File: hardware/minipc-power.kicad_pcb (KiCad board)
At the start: 4 copper layers, 52 x 36 mm, 106 parts, among them J1 USB-C HRO TYPE-C-31-M-12, J10 VSYS (switch), J11 CHG, J12 PG_CHG, J13 VBAT_SENSE, J14 3V3_PG, J15 GND, J16 GND, J17 GND, J2 BAT+, J3 BAT-, J4 NTC, J5 NTC-, J6 +12V OUT, J7 +5V OUT, J8 +3V3 OUT, J9 EN (switch), Q1 DMN1004UFV, Q2 DMN1004UFV, Q3 DMN1004UFV, Q4 CSD25404Q3, Q5 CSD25404Q3, Q6 2N7002, U1 CH224Q, U2 BQ25606, U3 HY2113-MB1A, U4 TPS61178, U5 TPS61088-Q1, U6 TPS63802

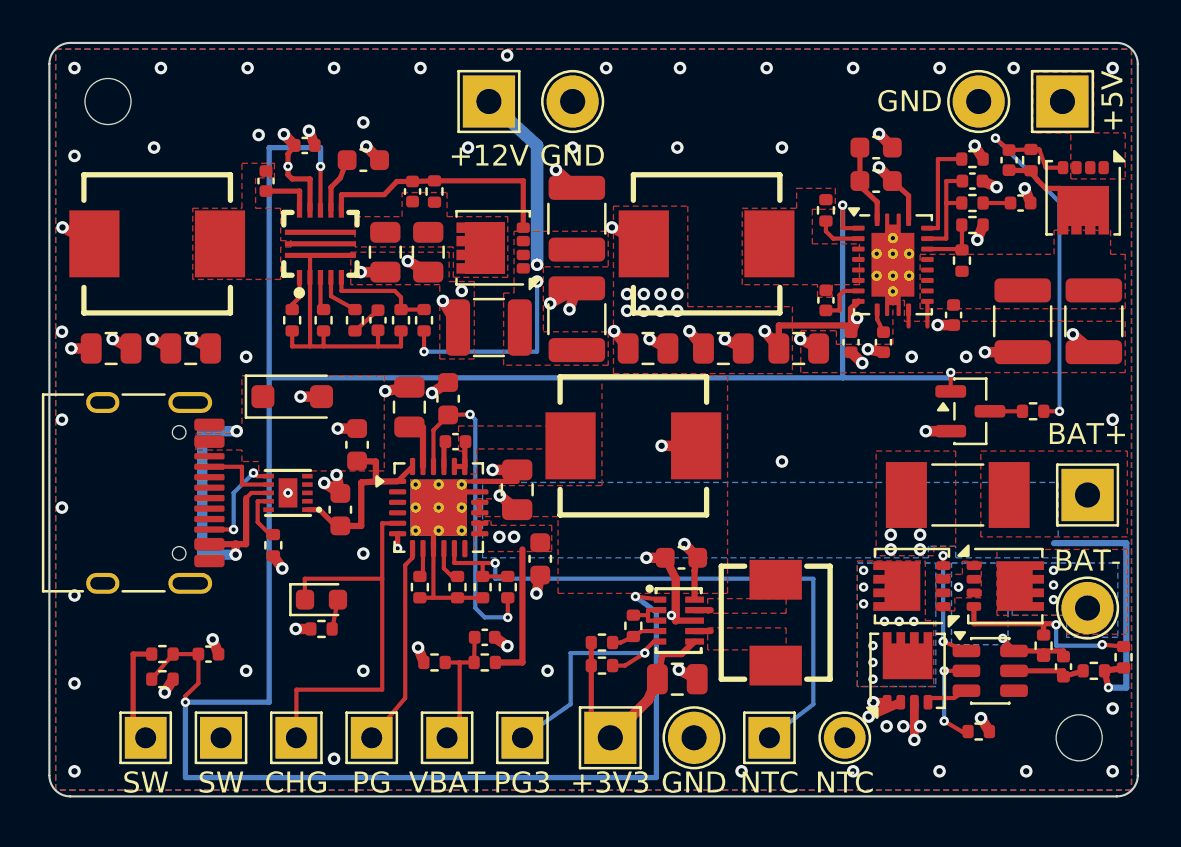
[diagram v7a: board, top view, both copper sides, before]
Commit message: Checks on kicad-skills e4b8240: sourcing.json, DRC exemption file, no vias on pads
docs/sourcing.json (JLCPCB, global warehouse, 5 boards) for the stock scripts (R24); docs/drc-accept.json names the
one accepted DRC item (J1's silk over the edge) for check.sh. routing.via_near keeps every via off every pad,
including the pad it stitches (board_lint flagged rings on C17/C18/C19/C31); stitch_pads falls back to a 0.45/0.2
via where a 0.6/0.3 with a mask web does not fit (C36). Schematic unchanged. DRC 0 (J1 silk accepted), ERC 0,
unconnected 0, parity 0, board_lint 0 problems (note: U1's exposed-pad via, deliberate), pins and fields clean.
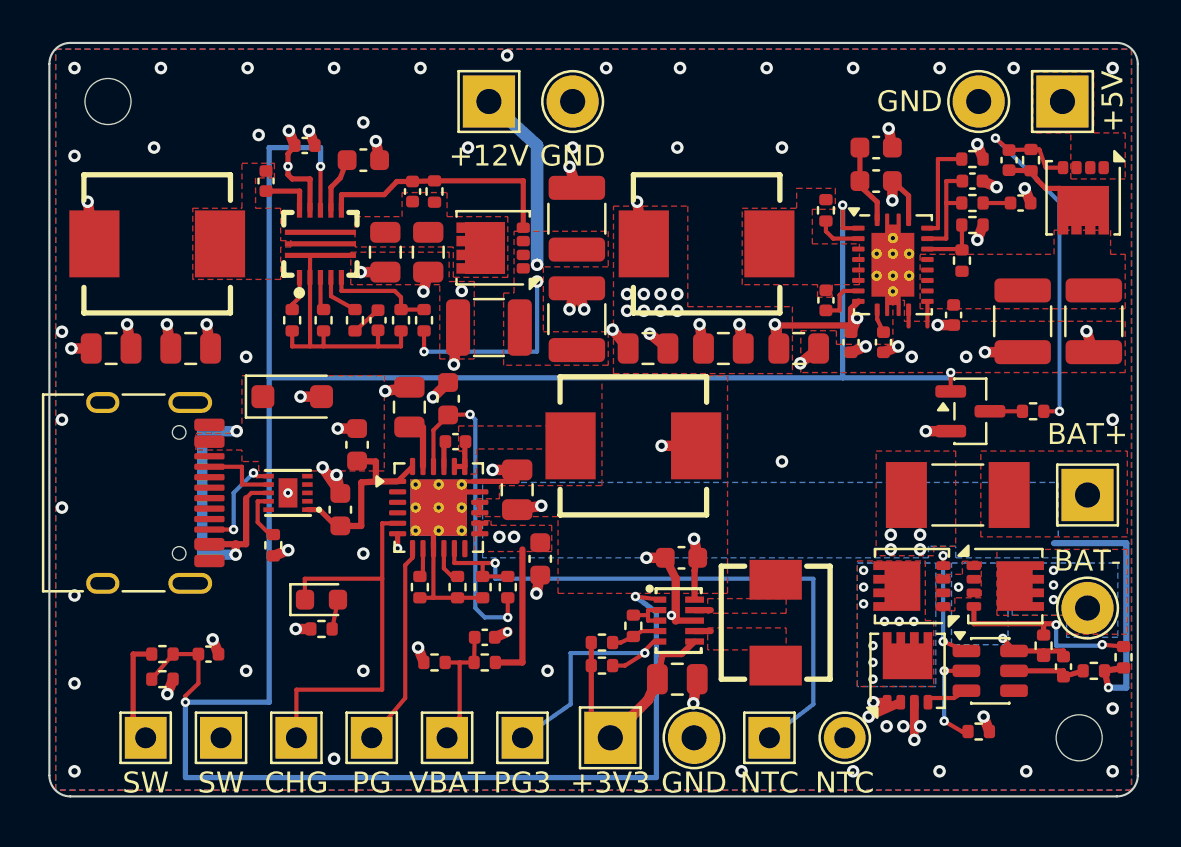
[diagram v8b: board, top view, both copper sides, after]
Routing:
- net VSYS: track 27.1 -> 28.4 mm
- net GND: track 77.1 -> 78.0 mm
